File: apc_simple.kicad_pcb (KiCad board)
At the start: 2 copper layers, 16 parts, among them J1 Output, J2 Power, U1 NE556

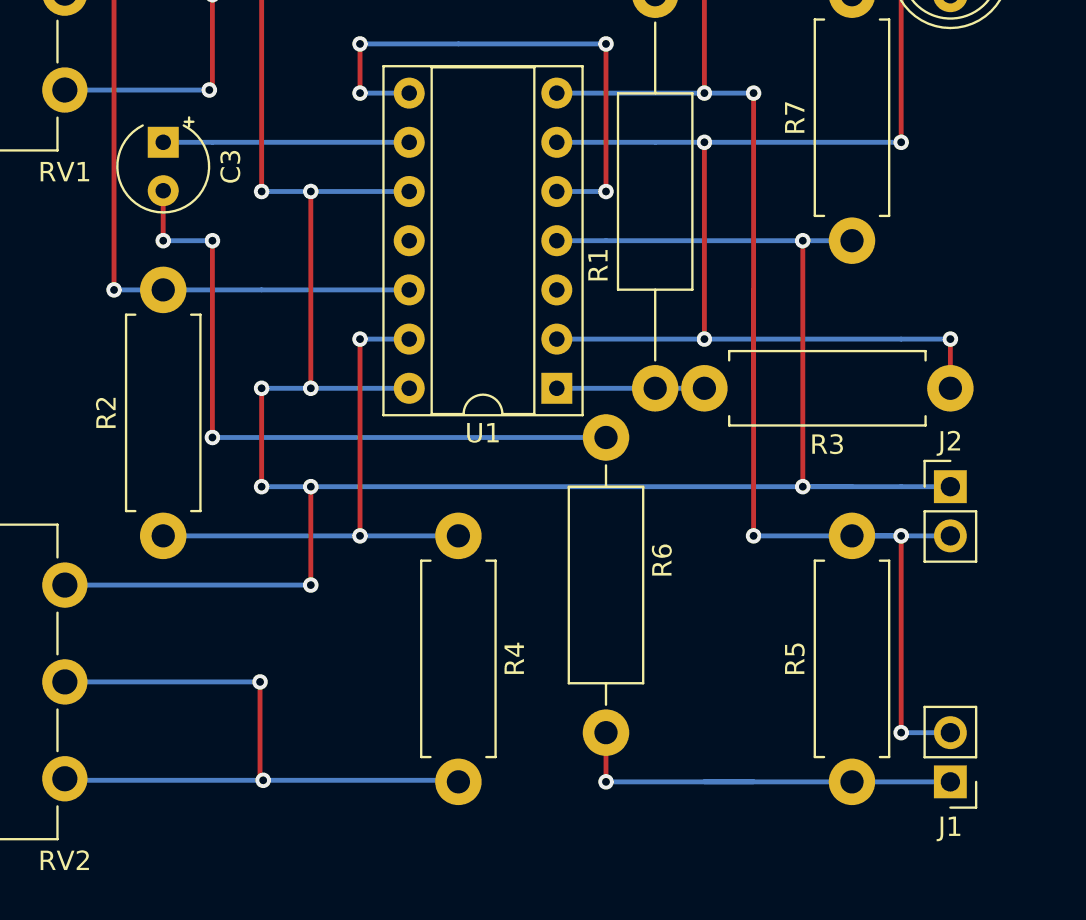
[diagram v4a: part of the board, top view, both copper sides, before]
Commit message: pcb: move pads to correct position
Modify C3, R3 and R6 footprints to match the
intended placement on a strip board.
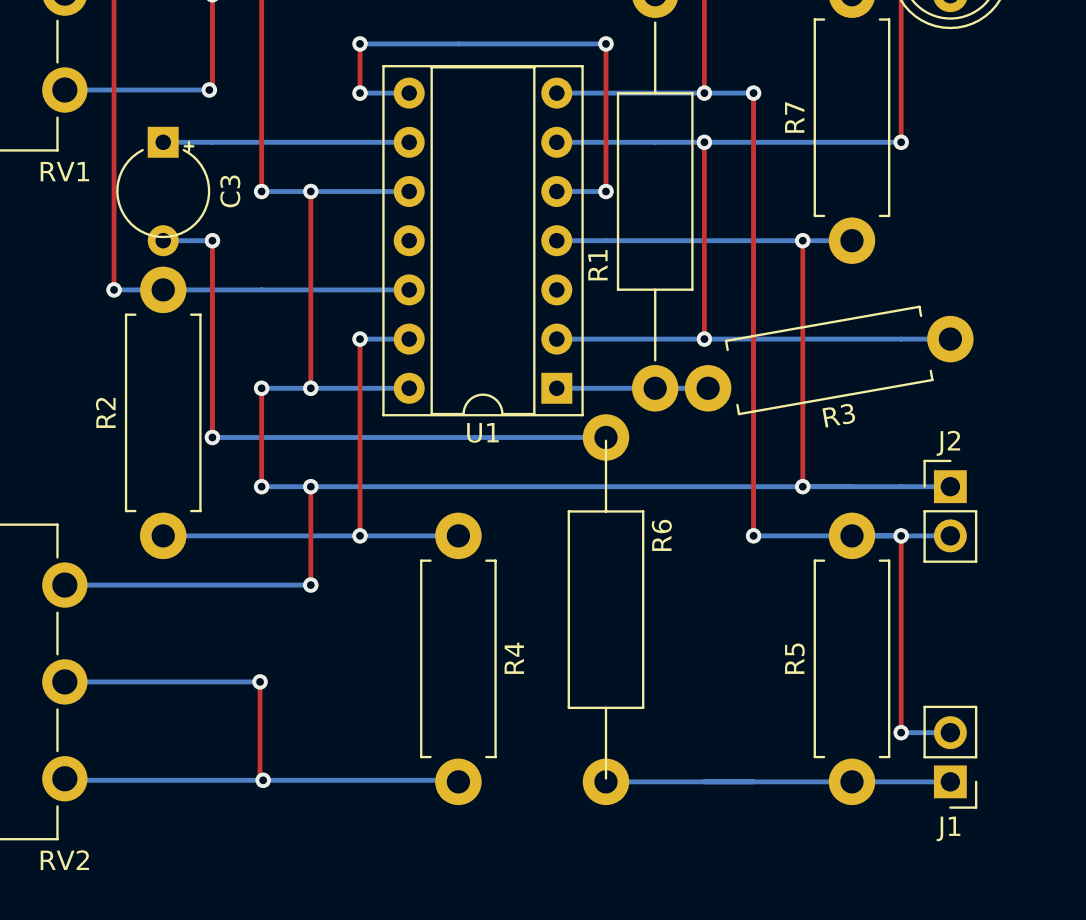
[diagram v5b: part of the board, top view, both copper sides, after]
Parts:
- R6: footprint Resistor_THT:R_Axial_DIN0411_L9.9mm_D3.6mm_P15.24mm_Horizontal -> Resistor_THT:R_Axial_DIN0411_L9.9mm_D3.6mm_P20.32mm_Horizontal
- moved R3 2.54 mm to (160.0, 99.1), turned to 190 degrees
- moved C3 1.27 mm to (119.4, 90.2)
- moved R6 1.27 mm to (142.2, 102.9)
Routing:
- net Net-(C3-Pad2): track 35.6 -> 33.0 mm, vias 3 -> 2
- net Net-(J1-Pad1): track 22.9 -> 20.3 mm, vias 1 -> 0
- net Net-(C1-Pad2): track 83.8 -> 81.3 mm, vias 5 -> 4
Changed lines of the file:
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@@
     (thickness 1.6)
     (drawings 18)
-    (tracks 137)
+    (tracks 131)
     (zones 0)
     (modules 16)
@@
     (add_net "Net-(U1-Pad5)")
   )
-  (module Resistor_THT:R_Axial_DIN0411_L9.9mm_D3.6mm_P15.24mm_Horizontal (layer F.Cu)
-    (at 142.24 104.14 270)
-    (descr "Resistor, Axial_DIN0411 series, Axial, Horizontal, pin pitch=15.24mm, 1W, length*diameter=9.9*3.6mm^2")
-    (tags "Resistor Axial_DIN0411 series Axial Horizontal pin pitch 15.24mm 1W length 9.9mm diameter 3.6mm")
+  (module Resistor_THT:R_Axial_DIN0411_L9.9mm_D3.6mm_P20.32mm_Horizontal (layer F.Cu)
+    (at 142.24 102.87 270)
+    (descr "Resistor, Axial_DIN0411 series, Axial, Horizontal, pin pitch=20.32mm, 1W, length*diameter=9.9*3.6mm^2")
+    (tags "Resistor Axial_DIN0411 series Axial Horizontal pin pitch 20.32mm 1W length 9.9mm diameter 3.6mm")
     (fp_text reference R6 (at 6.35 -2.92 90) (layer F.SilkS)
       (effects (font (size 1 1) (thickness 0.15)))
@@
       (effects (font (size 1 1) (thickness 0.15)))
     )
-    (fp_line (start 2.67 -1.8) (end 2.67 1.8) (layer F.Fab) (width 0.1))
-    (fp_line (start 2.67 1.8) (end 12.57 1.8) (layer F.Fab) (width 0.1))
-    (fp_line (start 12.57 1.8) (end 12.57 -1.8) (layer F.Fab) (width 0.1))
-    (fp_line (start 12.57 -1.8) (end 2.67 -1.8) (layer F.Fab) (width 0.1))
-    (fp_line (start 0 0) (end 2.67 0) (layer F.Fab) (width 0.1))
-    (fp_line (start 15.24 0) (end 12.57 0) (layer F.Fab) (width 0.1))
-    (fp_line (start 2.55 -1.92) (end 2.55 1.92) (layer F.SilkS) (width 0.12))
-    (fp_line (start 2.55 1.92) (end 12.69 1.92) (layer F.SilkS) (width 0.12))
-    (fp_line (start 12.69 1.92) (end 12.69 -1.92) (layer F.SilkS) (width 0.12))
-    (fp_line (start 12.69 -1.92) (end 2.55 -1.92) (layer F.SilkS) (width 0.12))
-    (fp_line (start 1.44 0) (end 2.55 0) (layer F.SilkS) (width 0.12))
-    (fp_line (start 13.8 0) (end 12.69 0) (layer F.SilkS) (width 0.12))
+    (fp_line (start 5.21 -1.8) (end 5.21 1.8) (layer F.Fab) (width 0.1))
+    (fp_line (start 5.21 1.8) (end 15.11 1.8) (layer F.Fab) (width 0.1))
+    (fp_line (start 15.11 1.8) (end 15.11 -1.8) (layer F.Fab) (width 0.1))
+    (fp_line (start 15.11 -1.8) (end 5.21 -1.8) (layer F.Fab) (width 0.1))
+    (fp_line (start 0 0) (end 5.21 0) (layer F.Fab) (width 0.1))
+    (fp_line (start 20.32 0) (end 15.11 0) (layer F.Fab) (width 0.1))
+    (fp_line (start 5.09 -1.92) (end 5.09 1.92) (layer F.SilkS) (width 0.12))
+    (fp_line (start 5.09 1.92) (end 15.23 1.92) (layer F.SilkS) (width 0.12))
+    (fp_line (start 15.23 1.92) (end 15.23 -1.92) (layer F.SilkS) (width 0.12))
+    (fp_line (start 15.23 -1.92) (end 5.09 -1.92) (layer F.SilkS) (width 0.12))
+    (fp_line (start 1.44 0) (end 5.09 0) (layer F.SilkS) (width 0.12))
+    (fp_line (start 18.88 0) (end 15.23 0) (layer F.SilkS) (width 0.12))
     (fp_line (start -1.45 -2.05) (end -1.45 2.05) (layer F.CrtYd) (width 0.05))
-    (fp_line (start -1.45 2.05) (end 16.69 2.05) (layer F.CrtYd) (width 0.05))
-    (fp_line (start 16.69 2.05) (end 16.69 -2.05) (layer F.CrtYd) (width 0.05))
-    (fp_line (start 16.69 -2.05) (end -1.45 -2.05) (layer F.CrtYd) (width 0.05))
-    (pad 2 thru_hole oval (at 15.24 0 270) (size 2.4 2.4) (drill 1.2) (layers *.Cu *.Mask)
+    (fp_line (start -1.45 2.05) (end 21.77 2.05) (layer F.CrtYd) (width 0.05))
+    (fp_line (start 21.77 2.05) (end 21.77 -2.05) (layer F.CrtYd) (width 0.05))
+    (fp_line (start 21.77 -2.05) (end -1.45 -2.05) (layer F.CrtYd) (width 0.05))
+    (pad 2 thru_hole oval (at 19.05 0 270) (size 2.4 2.4) (drill 1.2) (layers *.Cu *.Mask)
       (net 13 "Net-(J1-Pad1)"))
-    (pad 1 thru_hole circle (at 0 0 270) (size 2.4 2.4) (drill 1.2) (layers *.Cu *.Mask)
+    (pad 1 thru_hole circle (at 1.27 0 270) (size 2.4 2.4) (drill 1.2) (layers *.Cu *.Mask)
       (net 4 "Net-(C3-Pad2)"))
-    (model ${KISYS3DMOD}/Resistor_THT.3dshapes/R_Axial_DIN0411_L9.9mm_D3.6mm_P15.24mm_Horizontal.wrl
+    (model ${KISYS3DMOD}/Resistor_THT.3dshapes/R_Axial_DIN0411_L9.9mm_D3.6mm_P20.32mm_Horizontal.wrl
       (at (xyz 0 0 0))
       (scale (xyz 1 1 1))
@@
   )
   (module Capacitor_THT:CP_Radial_Tantal_D4.5mm_P2.50mm (layer F.Cu)
-    (at 119.38 88.9 270)
+    (at 119.38 90.17 270)
     (descr "CP, Radial_Tantal series, Radial, pin pitch=2.50mm, , diameter=4.5mm, Tantal Electrolytic Capacitor, http://cdn-reichelt.de/documents/datenblatt/B300/TANTAL-TB-Serie%23.pdf")
     (tags "CP Radial_Tantal series Radial pin pitch 2.50mm  diameter 4.5mm Tantal Electrolytic Capacitor")
@@
     )
     (fp_arc (start 1.25 0) (end -0.869741 -1.06) (angle 306.864288) (layer F.SilkS) (width 0.12))
-    (pad 2 thru_hole circle (at 2.5 0 270) (size 1.6 1.6) (drill 0.8) (layers *.Cu *.Mask)
+    (pad 2 thru_hole circle (at 3.81 0 270) (size 1.6 1.6) (drill 0.8) (layers *.Cu *.Mask)
       (net 4 "Net-(C3-Pad2)"))
-    (pad 1 thru_hole rect (at 0 0 270) (size 1.6 1.6) (drill 0.8) (layers *.Cu *.Mask)
+    (pad 1 thru_hole rect (at -1.27 0 270) (size 1.6 1.6) (drill 0.8) (layers *.Cu *.Mask)
       (net 5 "Net-(C3-Pad1)"))
     (model ${KISYS3DMOD}/Capacitor_THT.3dshapes/CP_Radial_Tantal_D4.5mm_P2.50mm.wrl
@@
   )
   (module Resistor_THT:R_Axial_DIN0411_L9.9mm_D3.6mm_P12.70mm_Horizontal (layer F.Cu)
-    (at 160.02 101.6 180)
+    (at 160.02 99.06 190)
     (descr "Resistor, Axial_DIN0411 series, Axial, Horizontal, pin pitch=12.7mm, 1W, length*diameter=9.9*3.6mm^2")
     (tags "Resistor Axial_DIN0411 series Axial Horizontal pin pitch 12.7mm 1W length 9.9mm diameter 3.6mm")
-    (fp_text reference R3 (at 6.35 -2.92) (layer F.SilkS)
-      (effects (font (size 1 1) (thickness 0.15)))
-    )
-    (fp_text value 1k (at 6.35 2.92) (layer F.Fab)
+    (fp_text reference R3 (at 6.35 -2.92 10) (layer F.SilkS)
+      (effects (font (size 1 1) (thickness 0.15)))
+    )
+    (fp_text value 1k (at 6.35 2.92 10) (layer F.Fab)
       (effects (font (size 1 1) (thickness 0.15)))
     )
@@
     (fp_line (start 14.15 2.05) (end 14.15 -2.05) (layer F.CrtYd) (width 0.05))
     (fp_line (start 14.15 -2.05) (end -1.45 -2.05) (layer F.CrtYd) (width 0.05))
-    (fp_text user %R (at 6.35 0) (layer F.Fab)
-      (effects (font (size 1 1) (thickness 0.15)))
-    )
-    (pad 2 thru_hole oval (at 12.7 0 180) (size 2.4 2.4) (drill 1.2) (layers *.Cu *.Mask)
+    (fp_text user %R (at 6.35 0 10) (layer F.Fab)
+      (effects (font (size 1 1) (thickness 0.15)))
+    )
+    (pad 2 thru_hole oval (at 12.758114 -0.329584 190) (size 2.4 2.4) (drill 1.2) (layers *.Cu *.Mask)
       (net 7 "Net-(R1-Pad1)"))
-    (pad 1 thru_hole circle (at 0 0 180) (size 2.4 2.4) (drill 1.2) (layers *.Cu *.Mask)
+    (pad 1 thru_hole circle (at 0 0 190) (size 2.4 2.4) (drill 1.2) (layers *.Cu *.Mask)
       (net 1 "Net-(C1-Pad2)"))
     (model ${KISYS3DMOD}/Resistor_THT.3dshapes/R_Axial_DIN0411_L9.9mm_D3.6mm_P12.70mm_Horizontal.wrl
@@
   (segment (start 139.7 99.06) (end 157.48 99.06) (width 0.25) (layer B.Cu) (net 1))
   (segment (start 157.48 99.06) (end 160.02 99.06) (width 0.25) (layer B.Cu) (net 1))
-  (via (at 160.02 99.06) (size 0.8) (drill 0.4) (layers F.Cu B.Cu) (net 1))
-  (segment (start 160.02 99.06) (end 160.02 101.6) (width 0.25) (layer F.Cu) (net 1))
   (segment (start 139.74 86.32) (end 139.7 86.36) (width 0.25) (layer B.Cu) (net 2))
   (segment (start 157.48 109.22) (end 157.48 109.22) (width 0.25) (layer B.Cu) (net 2))
@@
   (segment (start 142.24 104.14) (end 121.92 104.14) (width 0.25) (layer B.Cu) (net 4))
   (via (at 121.92 93.98) (size 0.8) (drill 0.4) (layers F.Cu B.Cu) (net 4))
-  (segment (start 119.38 91.4) (end 119.38 93.98) (width 0.25) (layer F.Cu) (net 4))
   (segment (start 121.92 93.98) (end 119.38 93.98) (width 0.25) (layer B.Cu) (net 4))
   (segment (start 119.38 93.98) (end 119.38 93.98) (width 0.25) (layer B.Cu) (net 4))
-  (via (at 119.38 93.98) (size 0.8) (drill 0.4) (layers F.Cu B.Cu) (net 4))
   (segment (start 121.92 93.98) (end 121.92 104.14) (width 0.25) (layer F.Cu) (net 4))
   (segment (start 121.92 88.9) (end 132.08 88.9) (width 0.25) (layer B.Cu) (net 5))
@@
   (segment (start 142.24 121.92) (end 149.86 121.92) (width 0.25) (layer B.Cu) (net 13))
   (segment (start 160.02 121.92) (end 147.32 121.92) (width 0.25) (layer B.Cu) (net 13))
-  (segment (start 142.24 119.38) (end 142.24 121.92) (width 0.25) (layer F.Cu) (net 13))
   (segment (start 142.24 121.92) (end 142.24 121.92) (width 0.25) (layer F.Cu) (net 13))
-  (via (at 142.24 121.92) (size 0.8) (drill 0.4) (layers F.Cu B.Cu) (net 13))
   (segment (start 160.02 81.28) (end 154.94 81.28) (width 0.25) (layer B.Cu) (net 14))
   (segment (start 139.7 91.44) (end 142.24 91.44) (width 0.25) (layer B.Cu) (net 15))
